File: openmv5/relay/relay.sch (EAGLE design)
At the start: 73 parts, among them IC1 TPS613222ADBVR, IC2 AP64060WU-7, IC3 LM321LVIDCKR, IC4 74LVC1G07GW,125, J1 OPENMV5-TOP, J2 1771088, K1 IMC03TS, K2 IMC03TS, Q1 SSM3J356R,LF, Q2 2N7002KW_R1_00001, Q3 2N7002KW_R1_00001, U1 74LVC1G17SE-7

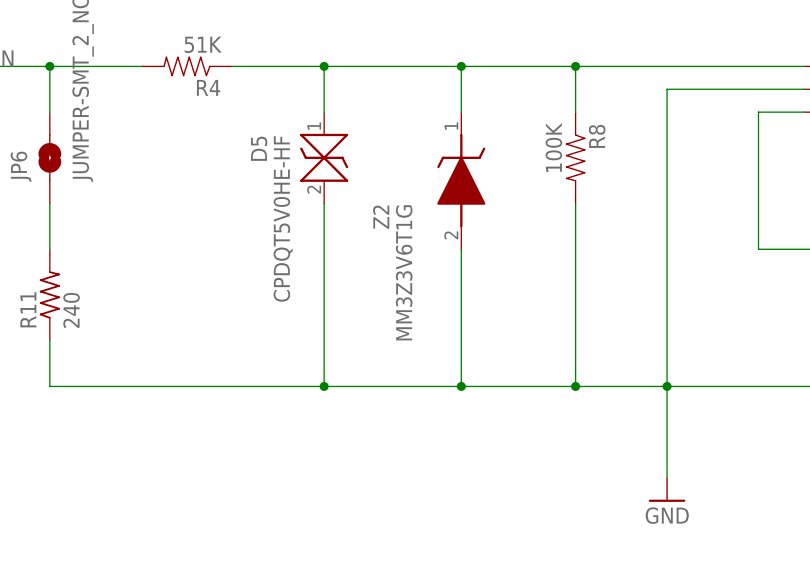
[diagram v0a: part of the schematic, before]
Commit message: Remove zener diode from ADC circuit
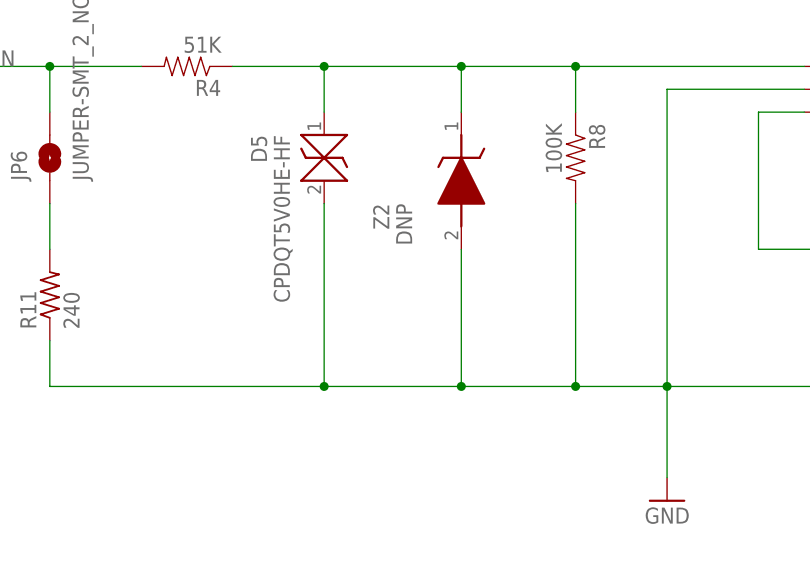
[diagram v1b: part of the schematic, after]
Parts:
- Z2: value MM3Z3V6T1G -> DNP; POPULATE (none) -> 0
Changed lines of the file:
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@@
 </part>
 <part name="GND7" library="sfe" deviceset="GND" device=""/>
-<part name="Z2" library="MM3Z3V6T1G" deviceset="MM3Z3V6T1G" device="">
+<part name="Z2" library="MM3Z3V6T1G" deviceset="MM3Z3V6T1G" device="" value="DNP">
 <attribute name="MPN" value="MM3Z3V6T1G"/>
+<attribute name="POPULATE" value="0"/>
 </part>
 <part name="R11" library="rcl" library_urn="urn:adsk.eagle:library:334" deviceset="R-US_" device="R0603" package3d_urn="urn:adsk.eagle:package:23555/3" value="240">
@@
 <attribute name="VALUE" x="308.61" y="233.68" size="1.778" layer="96" rot="MR270" align="center-left"/>
 <attribute name="MPN" x="314.96" y="243.84" size="1.778" layer="96" rot="MR270" display="off"/>
+<attribute name="POPULATE" x="314.96" y="243.84" size="1.778" layer="96" rot="MR270" display="off"/>
 </instance>
 <instance part="R11" gate="G$1" x="269.24" y="223.52" smashed="yes" rot="R90">
